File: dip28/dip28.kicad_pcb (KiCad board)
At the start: 2 copper layers, 30 x 63 mm, 8 parts, among them J1 PinHeader_1x06_P2.54mm_Horizo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, U1 ATmega328-P, Y1 16MHz

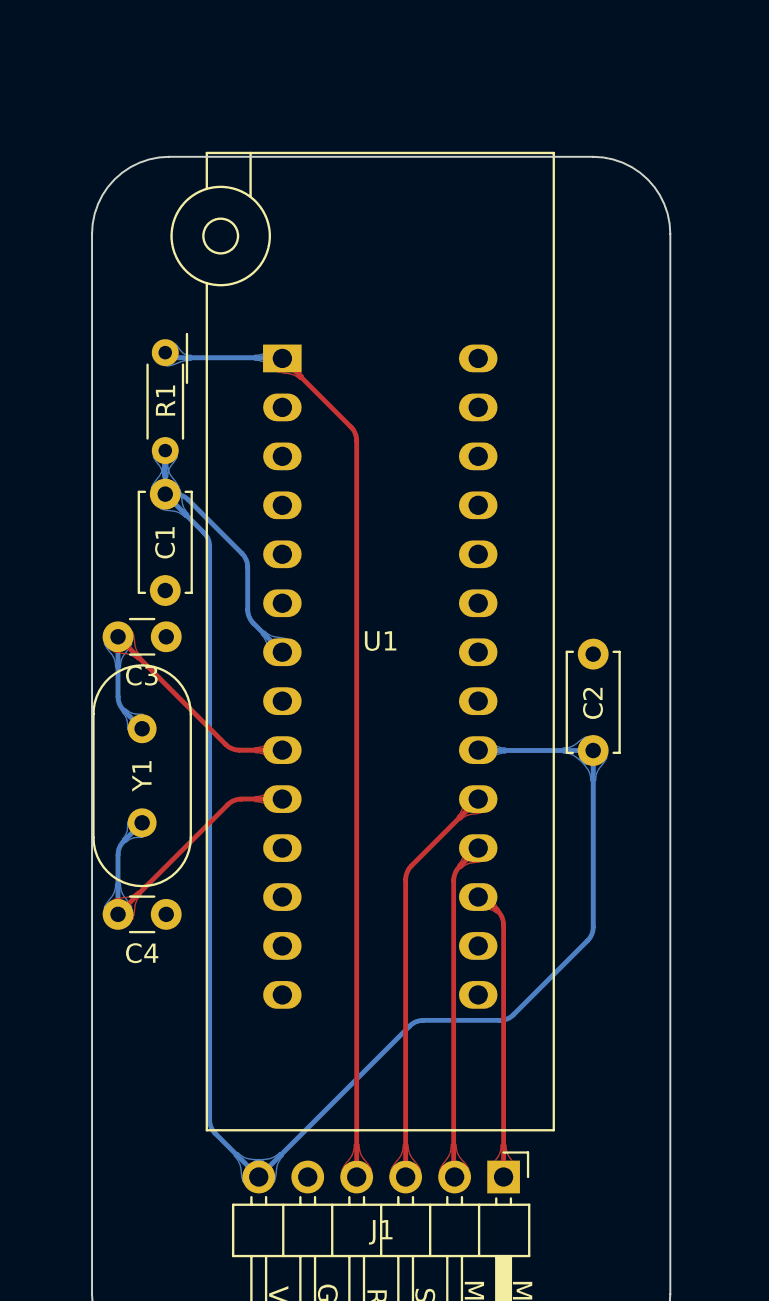
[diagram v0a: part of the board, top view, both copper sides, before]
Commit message: fixed pogo and dip adapter
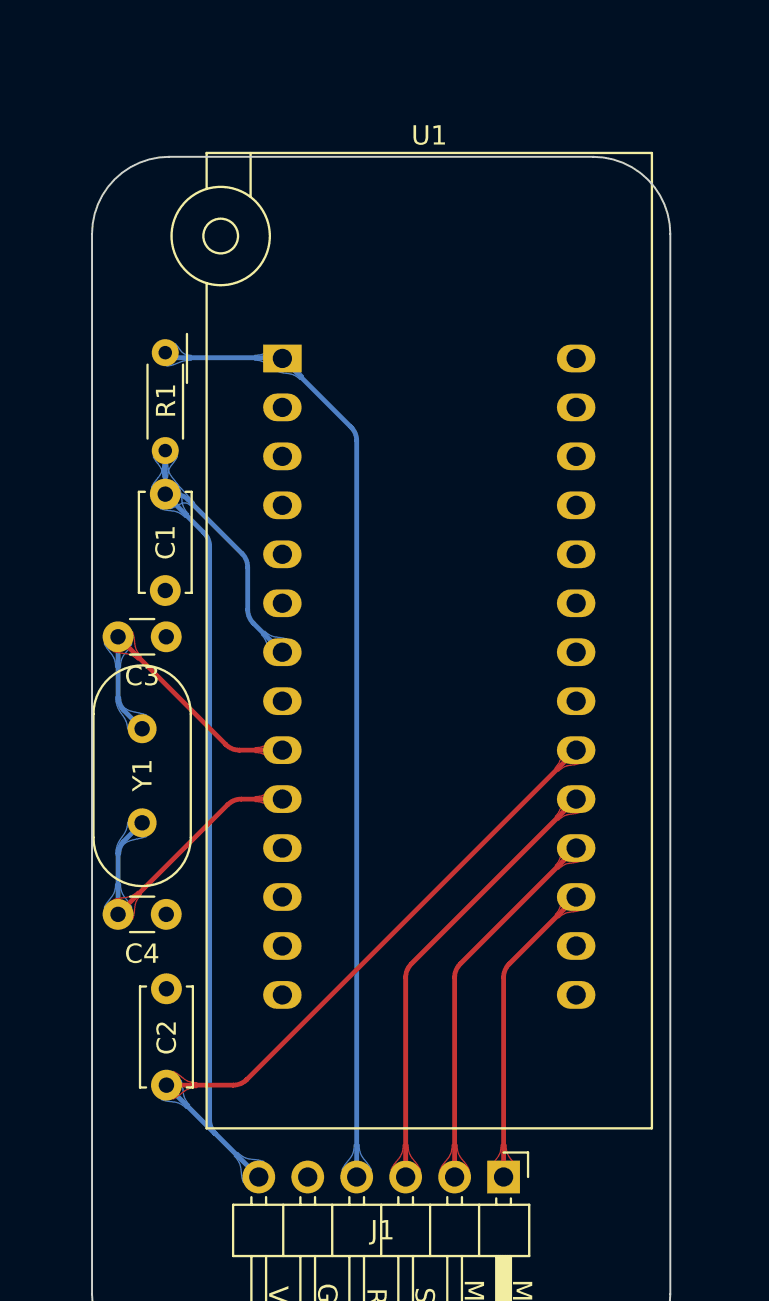
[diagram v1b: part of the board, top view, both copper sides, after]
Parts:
- U1: footprint Socket:DIP_Socket-28_W6.9_W7.62_W10.16_W12.7_W13.5_3M_228-4817-00-0602J -> Socket:DIP_Socket-28_W11.9_W12.7_W15.24_W17.78_W18.5_3M_228-1277-00-0602J
- moved C2 28.1 mm to (105.9, 150.7)
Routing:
- net +5V: track 88.6 -> 82.7 mm
- net SCK: track 21.1 -> 23.2 mm
- net MISO: track 17.6 -> 19.6 mm
- net MOSI: track 15.2 -> 16.0 mm
